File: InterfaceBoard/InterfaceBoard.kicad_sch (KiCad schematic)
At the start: 6 parts

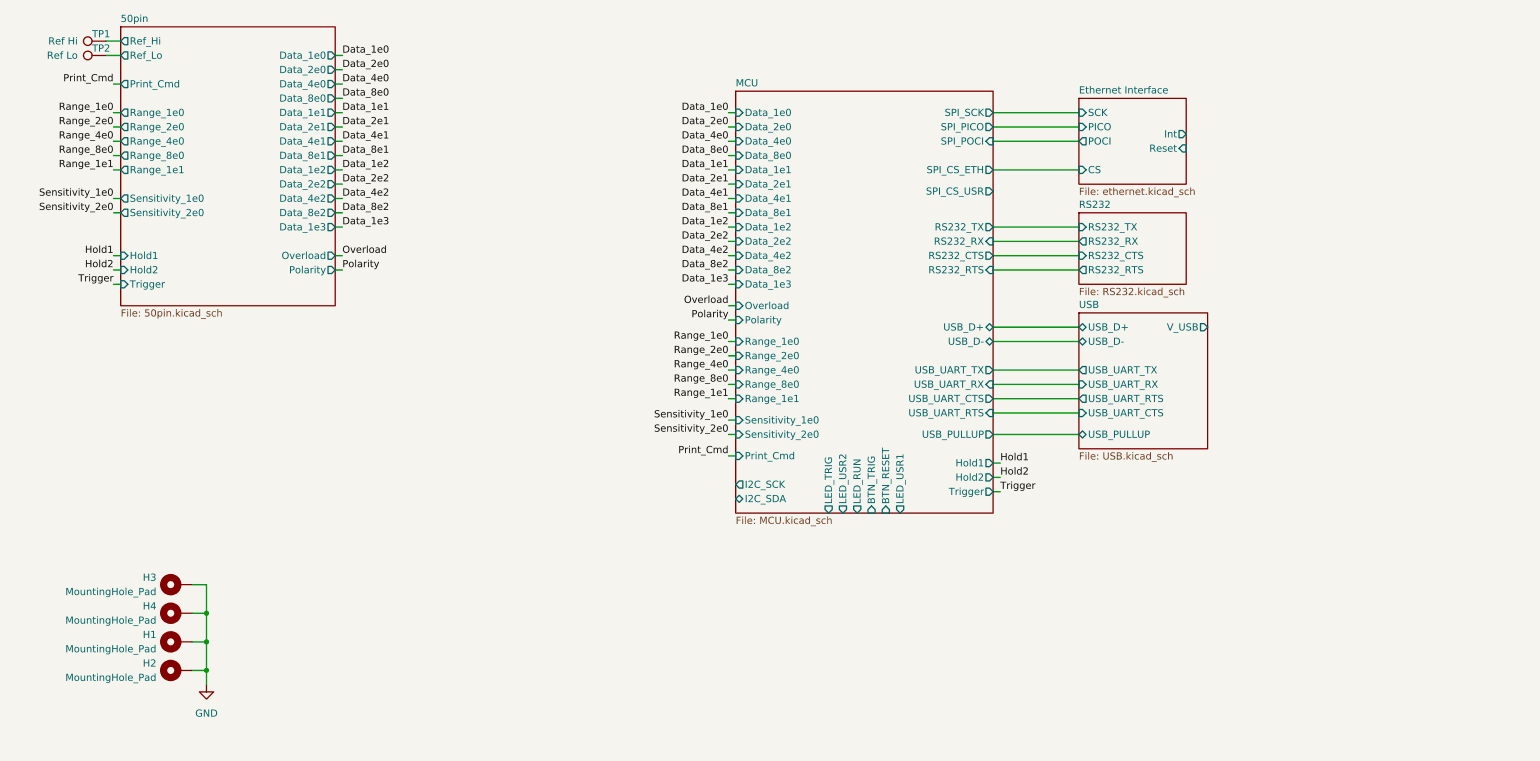
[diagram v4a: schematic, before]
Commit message: InterfaceBoard: Add 3.3 V regulater, test points.
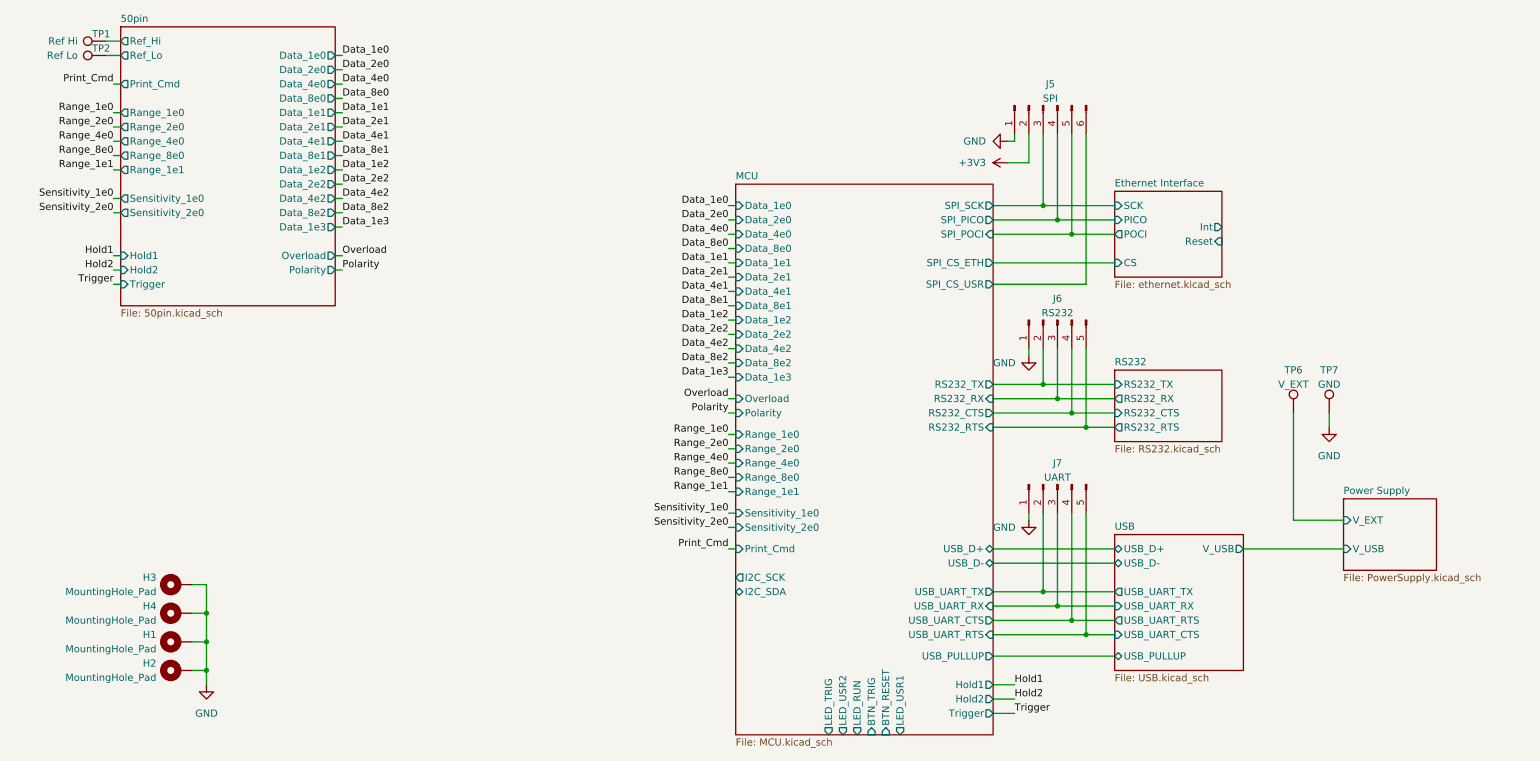
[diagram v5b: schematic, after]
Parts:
- added J5: SPI, Connector_PinHeader_1.27mm:PinHeader_1x06_P1.27mm_Vertical, symbol Connector:Conn_01x06_Male
- added J6: RS232, Connector_PinHeader_1.27mm:PinHeader_1x05_P1.27mm_Vertical, symbol Connector:Conn_01x05_Male
- added J7: UART, Connector_PinHeader_1.27mm:PinHeader_1x05_P1.27mm_Vertical, symbol Connector:Conn_01x05_Male
- added TP6: V_EXT, TestPoint:TestPoint_THTPad_2.0x2.0mm_Drill1.0mm, symbol Connector:TestPoint
- added TP7: GND, TestPoint:TestPoint_THTPad_2.0x2.0mm_Drill1.0mm, symbol Connector:TestPoint
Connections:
- net Ethernet Interface/PICO: now also J5.4 (Pin_4)
- net Ethernet Interface/POCI: now also J5.5 (Pin_5)
- net Ethernet Interface/SCK: now also J5.3 (Pin_3)
- net GND: now also J5.1 (Pin_1), J6.1 (Pin_1), J7.1 (Pin_1), TP7.1
- net MCU/RS232_CTS: now also J6.4 (Pin_4)
- net MCU/RS232_RTS: now also J6.5 (Pin_5)
- net MCU/RS232_RX: now also J6.3 (Pin_3)
- net MCU/RS232_TX: now also J6.2 (Pin_2)
- net MCU/SPI_CS_USR: now also J5.6 (Pin_6)
- net MCU/USB_UART_CTS: now also J7.4 (Pin_4)
- net MCU/USB_UART_RTS: now also J7.5 (Pin_5)
- net MCU/USB_UART_RX: now also J7.3 (Pin_3)
- net MCU/USB_UART_TX: now also J7.2 (Pin_2)
- new net +3V3: J5.2 (Pin_2)
- new net Power Supply/V_EXT: TP6.1
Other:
- added sheet Power Supply (PowerSupply.kicad_sch)

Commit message: InterfaceBoard: Routed some digital interfaces to MCU
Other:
- sheet MCU ports: added ETH_INT, ETH_RESET; removed none
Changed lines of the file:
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@@
+    (stroke (width 0) (type default) (color 0 0 0 0))
+  )
+  (wire (pts (xy 228.6 55.88) (xy 224.79 55.88))
     (stroke (width 0) (type default) (color 0 0 0 0))
   )
@@
     (stroke (width 0) (type default) (color 0 0 0 0))
   )
+  (wire (pts (xy 227.33 25.4) (xy 227.33 53.34))
+    (stroke (width 0) (type default) (color 0 0 0 0))
+  )
   (wire (pts (xy 193.04 104.14) (xy 193.04 118.11))
     (stroke (width 0) (type default) (color 0 0 0 0))
@@
     (stroke (width 0) (type default) (color 0 0 0 0))
   )
+  (wire (pts (xy 168.91 45.72) (xy 168.91 25.4))
+    (stroke (width 0) (type default) (color 0 0 0 0))
+  )
   (wire (pts (xy 198.12 54.61) (xy 205.74 54.61))
     (stroke (width 0) (type default) (color 0 0 0 0))
@@
     (stroke (width 0) (type default) (color 0 0 0 0))
   )
+  (wire (pts (xy 228.6 24.13) (xy 228.6 55.88))
+    (stroke (width 0) (type default) (color 0 0 0 0))
+  )
   (wire (pts (xy 41.91 132.08) (xy 44.45 132.08))
     (stroke (width 0) (type default) (color 0 0 0 0))
@@
     (stroke (width 0) (type default) (color 0 0 0 0))
   )
+  (wire (pts (xy 227.33 53.34) (xy 224.79 53.34))
+    (stroke (width 0) (type default) (color 0 0 0 0))
+  )
   (wire (pts (xy 27.94 38.1) (xy 29.21 38.1))
     (stroke (width 0) (type default) (color 0 0 0 0))
@@
     (stroke (width 0) (type default) (color 0 0 0 0))
   )
+  (wire (pts (xy 166.37 24.13) (xy 228.6 24.13))
+    (stroke (width 0) (type default) (color 0 0 0 0))
+  )
   (wire (pts (xy 243.84 86.36) (xy 243.84 88.9))
     (stroke (width 0) (type default) (color 0 0 0 0))
@@
     (stroke (width 0) (type default) (color 0 0 0 0))
   )
+  (wire (pts (xy 168.91 25.4) (xy 227.33 25.4))
+    (stroke (width 0) (type default) (color 0 0 0 0))
+  )
   (wire (pts (xy 138.43 57.15) (xy 137.16 57.15))
     (stroke (width 0) (type default) (color 0 0 0 0))
@@
   )
   (wire (pts (xy 138.43 72.39) (xy 137.16 72.39))
+    (stroke (width 0) (type default) (color 0 0 0 0))
+  )
+  (wire (pts (xy 166.37 45.72) (xy 166.37 24.13))
     (stroke (width 0) (type default) (color 0 0 0 0))
   )
@@
     )
     (pin "USB_PULLUP" output (at 184.15 129.54 0)
+      (effects (font (size 1.27 1.27)) (justify right))
+    )
+    (pin "ETH_INT" input (at 168.91 45.72 90)
+      (effects (font (size 1.27 1.27)) (justify right))
+    )
+    (pin "ETH_RESET" input (at 166.37 45.72 90)
       (effects (font (size 1.27 1.27)) (justify right))
     )
@@
       (reference "#PWR0184") (unit 1) (value "GND") (footprint "")
     )
+    (path "/e4ed5f74-a53b-42a4-9a6a-98aac2ab5b90/dc06d16e-5c9c-417d-ab4b-f51ad0c315db"
+      (reference "#PWR0185") (unit 1) (value "+3V3") (footprint "")
+    )
+    (path "/e4ed5f74-a53b-42a4-9a6a-98aac2ab5b90/a6fc5ea2-f942-4399-9a20-e2c5f8082f0f"
+      (reference "#PWR0186") (unit 1) (value "GND") (footprint "")
+    )
     (path "/7510d84d-561c-4c04-9a47-602785bf143f/33265ba7-ef1d-49c8-b2f9-33fbd5dfa7c1"
       (reference "C1") (unit 1) (value "10nF") (footprint "Capacitor_SMD:C_0603_1608Metric")
@@
       (reference "D7") (unit 1) (value "PE1605M1Q") (footprint "Diode_SMD:D_0402_1005Metric")
     )
+    (path "/e4ed5f74-a53b-42a4-9a6a-98aac2ab5b90/13222c49-f901-4ac9-8353-92eed0535f2e"
+      (reference "D8") (unit 1) (value "Red") (footprint "LED_SMD:LED_0603_1608Metric")
+    )
     (path "/7510d84d-561c-4c04-9a47-602785bf143f/9967f107-894f-4df6-9386-1ee530fb00e3"
       (reference "FB1") (unit 1) (value "1k") (footprint "Inductor_SMD:L_0805_2012Metric")
@@
       (reference "R84") (unit 1) (value "10k") (footprint "Resistor_SMD:R_0603_1608Metric")
     )
+    (path "/e4ed5f74-a53b-42a4-9a6a-98aac2ab5b90/0294e078-8e75-426e-92d7-e583a57dc66e"
+      (reference "R85") (unit 1) (value "1k") (footprint "Resistor_SMD:R_0603_1608Metric")
+    )
     (path "/6b1005e4-cf6f-4a1d-aca2-678196de2d73"
